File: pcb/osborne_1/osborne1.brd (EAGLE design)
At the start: 40 x 97 mm, 20 parts, among them J2 ATX24RH

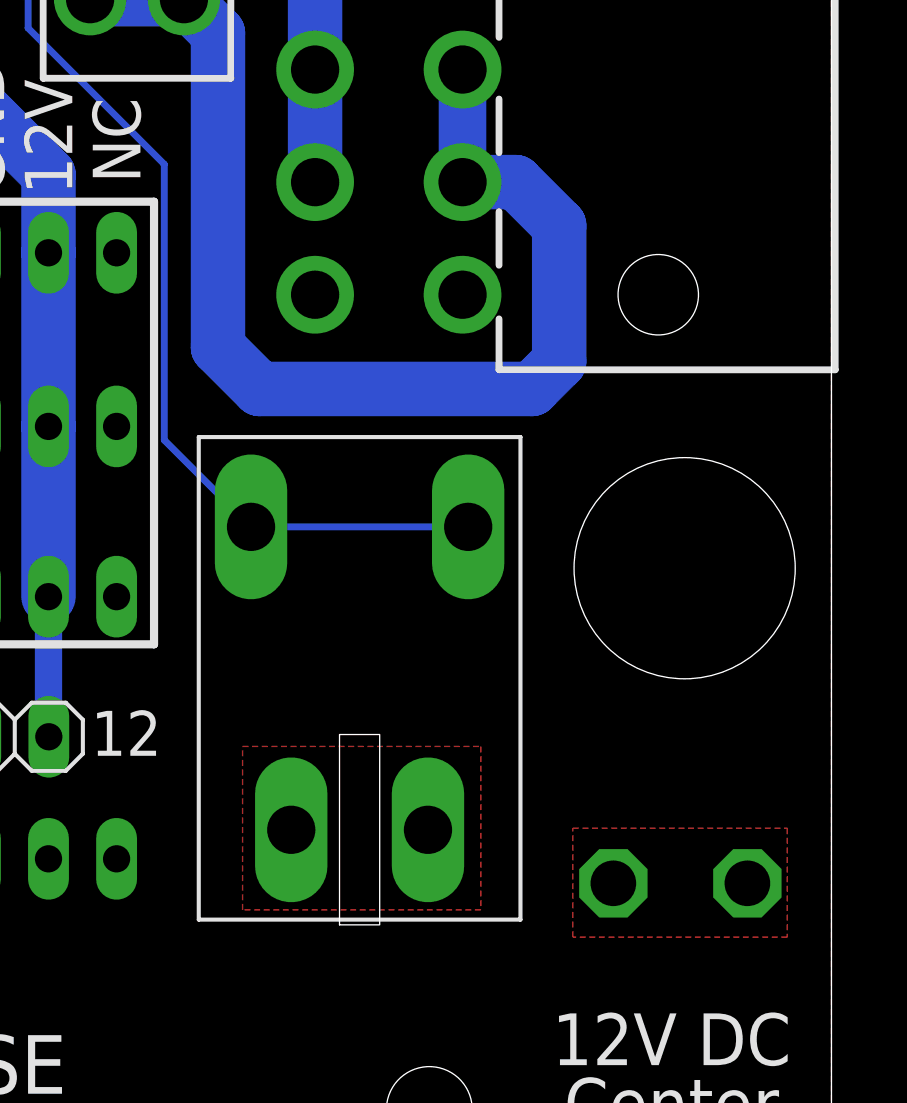
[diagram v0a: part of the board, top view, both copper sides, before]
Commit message: adjusted switch position
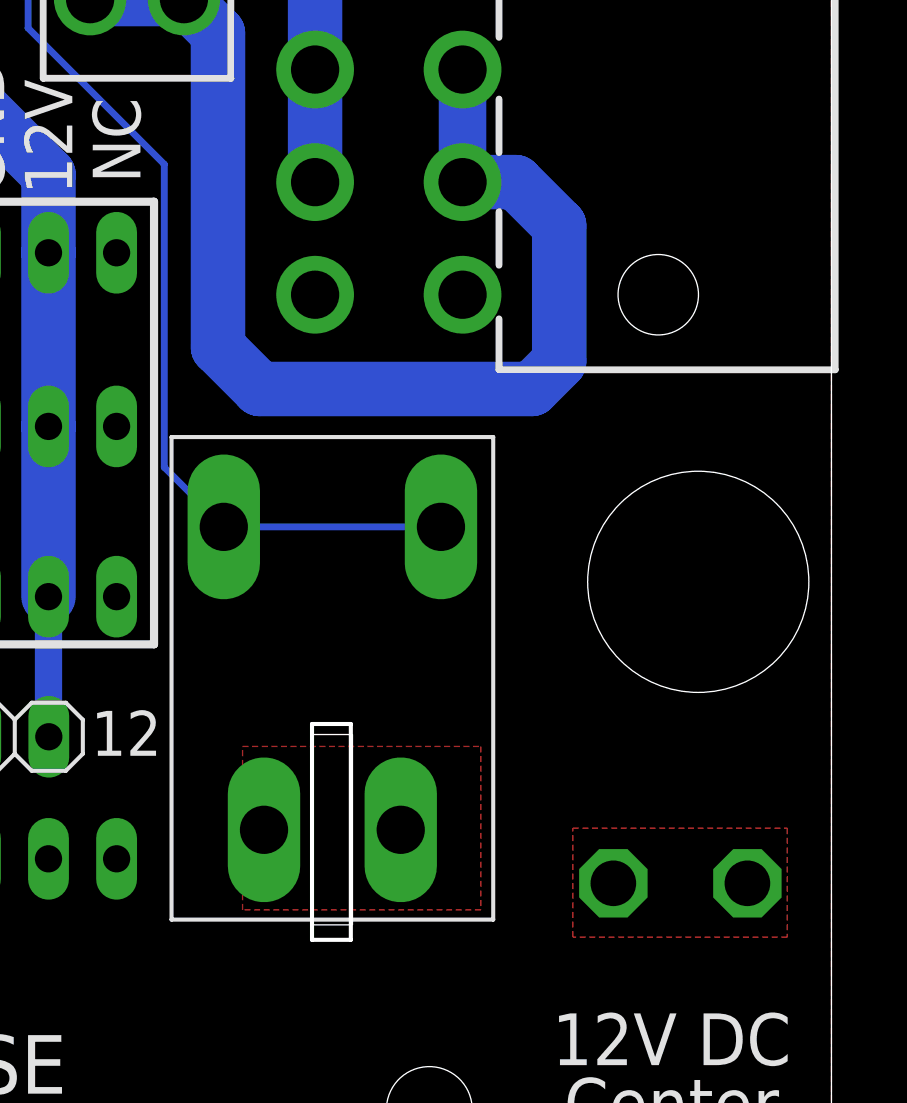
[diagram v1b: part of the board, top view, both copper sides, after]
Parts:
- moved U$4 1.02 mm to (21.4, 21.1)
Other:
- outline, holes or cut-outs redrawn
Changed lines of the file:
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@@
 <setting verticaltext="up"/>
 </settings>
-<grid distance="5" unitdist="mil" unit="mil" style="lines" multiple="1" display="no" altdistance="1" altunitdist="mil" altunit="mil"/>
+<grid distance="1" unitdist="mil" unit="mil" style="lines" multiple="1" display="no" altdistance="1" altunitdist="mil" altunit="mil"/>
 <layers>
 <layer number="1" name="Top" color="4" fill="1" visible="yes" active="yes"/>
@@
 <layer number="43" name="vRestrict" color="2" fill="10" visible="no" active="yes"/>
 <layer number="44" name="Drills" color="7" fill="1" visible="no" active="yes"/>
-<layer number="45" name="Holes" color="7" fill="1" visible="no" active="yes"/>
+<layer number="45" name="Holes" color="7" fill="1" visible="yes" active="yes"/>
 <layer number="46" name="Milling" color="3" fill="1" visible="yes" active="yes"/>
 <layer number="47" name="Measures" color="7" fill="1" visible="no" active="yes"/>
@@
 <text x="8.001" y="5.207" size="2.1844" layer="25" distance="35" align="center">FUSE
 5A MAX</text>
-<hole x="34.524" y="25.191" drill="8.25"/>
+<hole x="35.032" y="24.683" drill="8.25"/>
 <wire x1="45" y1="10" x2="-5" y2="10" width="0.1524" layer="51"/>
 <wire x1="0" y1="87" x2="87" y2="87" width="0.1524" layer="51"/>
@@
 <wire x1="4.318" y1="22.352" x2="4.318" y2="38.862" width="0.3048" layer="21"/>
 <text x="5.334" y="57.15" size="2.1844" layer="25" distance="35" rot="R90" align="center">+</text>
+<polygon width="0.1524" layer="46">
+<vertex x="20.6248" y="19.3802"/>
+<vertex x="22.0726" y="19.3802"/>
+<vertex x="22.0726" y="11.3284"/>
+<vertex x="20.6248" y="11.3284"/>
+</polygon>
 </plain>
 <attributes>
@@
 <element name="U$1" library="a" package="M3_MOUNTING_HOLE_PACK" value="M3_MOUNTING_HOLE" x="25" y="92" smashed="yes"/>
 <element name="U$3" library="a" package="M3_MOUNTING_HOLE_PACK" value="M3_MOUNTING_HOLE" x="25" y="5" smashed="yes"/>
-<element name="U$4" library="atx4vc" package="ROCK_SWITCH_VERTICAL" value="ROCK_SWRSW_VERTICAL" x="22.4" y="21.083" smashed="yes" rot="R90"/>
+<element name="U$4" library="atx4vc" package="ROCK_SWITCH_VERTICAL" value="ROCK_SWRSW_VERTICAL" x="21.384" y="21.083" smashed="yes" rot="R90"/>
 <element name="JP1" library="appleii" package="1X04" value="" x="9.525" y="24.13" smashed="yes" rot="MR180"/>
 <element name="JP2" library="appleii" package="1X04" value="" x="9.525" y="30.48" smashed="yes" rot="MR180"/>
@@
 <wire x1="15.621" y1="50.038" x2="11.176" y2="50.038" width="0.254" layer="16"/>
 <wire x1="11.176" y1="50.038" x2="10.033" y2="48.895" width="0.254" layer="16"/>
-<wire x1="15.113" y1="29.97" x2="18.35" y2="26.733" width="0.254" layer="16"/>
+<wire x1="15.113" y1="28.954" x2="17.334" y2="26.733" width="0.254" layer="16"/>
 <wire x1="10.033" y1="48.895" x2="10.033" y2="45.339" width="0.254" layer="16"/>
 <wire x1="10.033" y1="45.339" x2="15.113" y2="40.259" width="0.254" layer="16"/>
-<wire x1="15.113" y1="40.259" x2="15.113" y2="29.97" width="0.254" layer="16"/>
-<wire x1="18.35" y1="26.733" x2="26.45" y2="26.733" width="0.254" layer="16"/>
+<wire x1="15.113" y1="40.259" x2="15.113" y2="28.954" width="0.254" layer="16"/>
+<wire x1="17.334" y1="26.733" x2="25.434" y2="26.733" width="0.254" layer="16"/>
 </signal>
 <signal name="N$3">

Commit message: updated PCB
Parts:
- moved U$4 0.51 mm to (20.9, 21.1)
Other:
- outline, holes or cut-outs redrawn
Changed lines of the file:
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@@
 <setting verticaltext="up"/>
 </settings>
-<grid distance="1" unitdist="mil" unit="mil" style="lines" multiple="1" display="no" altdistance="1" altunitdist="mil" altunit="mil"/>
+<grid distance="20" unitdist="mil" unit="mil" style="lines" multiple="1" display="no" altdistance="1" altunitdist="mil" altunit="mil"/>
 <layers>
 <layer number="1" name="Top" color="4" fill="1" visible="yes" active="yes"/>
@@
 <text x="8.001" y="5.207" size="2.1844" layer="25" distance="35" align="center">FUSE
 5A MAX</text>
-<hole x="35.032" y="24.683" drill="8.25"/>
+<hole x="35.052" y="25.146" drill="8.25"/>
 <wire x1="45" y1="10" x2="-5" y2="10" width="0.1524" layer="51"/>
 <wire x1="0" y1="87" x2="87" y2="87" width="0.1524" layer="51"/>
@@
 <text x="8.255" y="41.656" size="1.778" layer="25" rot="R270" align="center">GND</text>
 <text x="13.335" y="41.148" size="1.778" layer="25" rot="R270" align="center">NC</text>
-<text x="9.144" y="48.26" size="1.778" layer="25" rot="R270" align="center">12V</text>
+<text x="9.144" y="47.752" size="1.9304" layer="25" rot="R270" align="center">12V</text>
 <text x="5.207" y="75.716" size="2.1844" layer="25" rot="R180" align="center">+</text>
 <text x="5.842" y="67.334" size="2.1844" layer="25" rot="R180" align="center">+</text>
@@
 <text x="5.334" y="57.15" size="2.1844" layer="25" distance="35" rot="R90" align="center">+</text>
 <polygon width="0.1524" layer="46">
-<vertex x="20.6248" y="19.3802"/>
-<vertex x="22.0726" y="19.3802"/>
-<vertex x="22.0726" y="11.3284"/>
-<vertex x="20.6248" y="11.3284"/>
+<vertex x="20.1168" y="19.8882"/>
+<vertex x="21.5646" y="19.8882"/>
+<vertex x="21.5646" y="11.3284"/>
+<vertex x="20.1168" y="11.3284"/>
 </polygon>
 </plain>
@@
 <element name="U$1" library="a" package="M3_MOUNTING_HOLE_PACK" value="M3_MOUNTING_HOLE" x="25" y="92" smashed="yes"/>
 <element name="U$3" library="a" package="M3_MOUNTING_HOLE_PACK" value="M3_MOUNTING_HOLE" x="25" y="5" smashed="yes"/>
-<element name="U$4" library="atx4vc" package="ROCK_SWITCH_VERTICAL" value="ROCK_SWRSW_VERTICAL" x="21.384" y="21.083" smashed="yes" rot="R90"/>
+<element name="U$4" library="atx4vc" package="ROCK_SWITCH_VERTICAL" value="ROCK_SWRSW_VERTICAL" x="20.876" y="21.083" smashed="yes" rot="R90"/>
 <element name="JP1" library="appleii" package="1X04" value="" x="9.525" y="24.13" smashed="yes" rot="MR180"/>
 <element name="JP2" library="appleii" package="1X04" value="" x="9.525" y="30.48" smashed="yes" rot="MR180"/>
@@
 </element>
 <element name="C1" library="capacitor-wima" library_urn="urn:adsk.eagle:library:116" package="C5B2.5" package3d_urn="urn:adsk.eagle:package:5426/1" value="" x="8.001" y="69.596" smashed="yes" rot="R90">
+<attribute name="NAME" x="5.969" y="69.596" size="1.27" layer="25" ratio="10" rot="R90"/>
 <attribute name="POPULARITY" value="10" x="8.001" y="69.596" size="1.778" layer="27" rot="R90" display="off"/>
 <attribute name="VALUE" x="10.795" y="67.564" size="1.27" layer="27" ratio="10" rot="R90"/>
@@
 <contactref element="C1" pad="2"/>
 <polygon width="0.2032" layer="1" thermals="no">
-<vertex x="18.034" y="18.542"/>
-<vertex x="26.924" y="18.542"/>
-<vertex x="26.924" y="12.446"/>
-<vertex x="18.034" y="12.446"/>
+<vertex x="16.51" y="18.542"/>
+<vertex x="25.4" y="18.542"/>
+<vertex x="25.4" y="12.446"/>
+<vertex x="16.51" y="12.446"/>
 </polygon>
 </signal>
@@
 <wire x1="15.621" y1="50.038" x2="11.176" y2="50.038" width="0.254" layer="16"/>
 <wire x1="11.176" y1="50.038" x2="10.033" y2="48.895" width="0.254" layer="16"/>
-<wire x1="15.113" y1="28.954" x2="17.334" y2="26.733" width="0.254" layer="16"/>
+<wire x1="15.113" y1="28.446" x2="16.826" y2="26.733" width="0.254" layer="16"/>
 <wire x1="10.033" y1="48.895" x2="10.033" y2="45.339" width="0.254" layer="16"/>
 <wire x1="10.033" y1="45.339" x2="15.113" y2="40.259" width="0.254" layer="16"/>
-<wire x1="15.113" y1="40.259" x2="15.113" y2="28.954" width="0.254" layer="16"/>
-<wire x1="17.334" y1="26.733" x2="25.434" y2="26.733" width="0.254" layer="16"/>
+<wire x1="15.113" y1="40.259" x2="15.113" y2="28.446" width="0.254" layer="16"/>
+<wire x1="16.826" y1="26.733" x2="24.926" y2="26.733" width="0.254" layer="16"/>
 </signal>
 <signal name="N$3">
